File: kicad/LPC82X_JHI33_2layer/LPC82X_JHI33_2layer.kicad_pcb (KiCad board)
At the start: 2 copper layers, 23.6 x 23.5 mm, 23 parts, among them J1 Conn_02x09_Odd_Even, J2 Conn_02x09_Odd_Even, J3 JTAG_2X05, U1 LPC824M201JHI33, Y1 12MHz

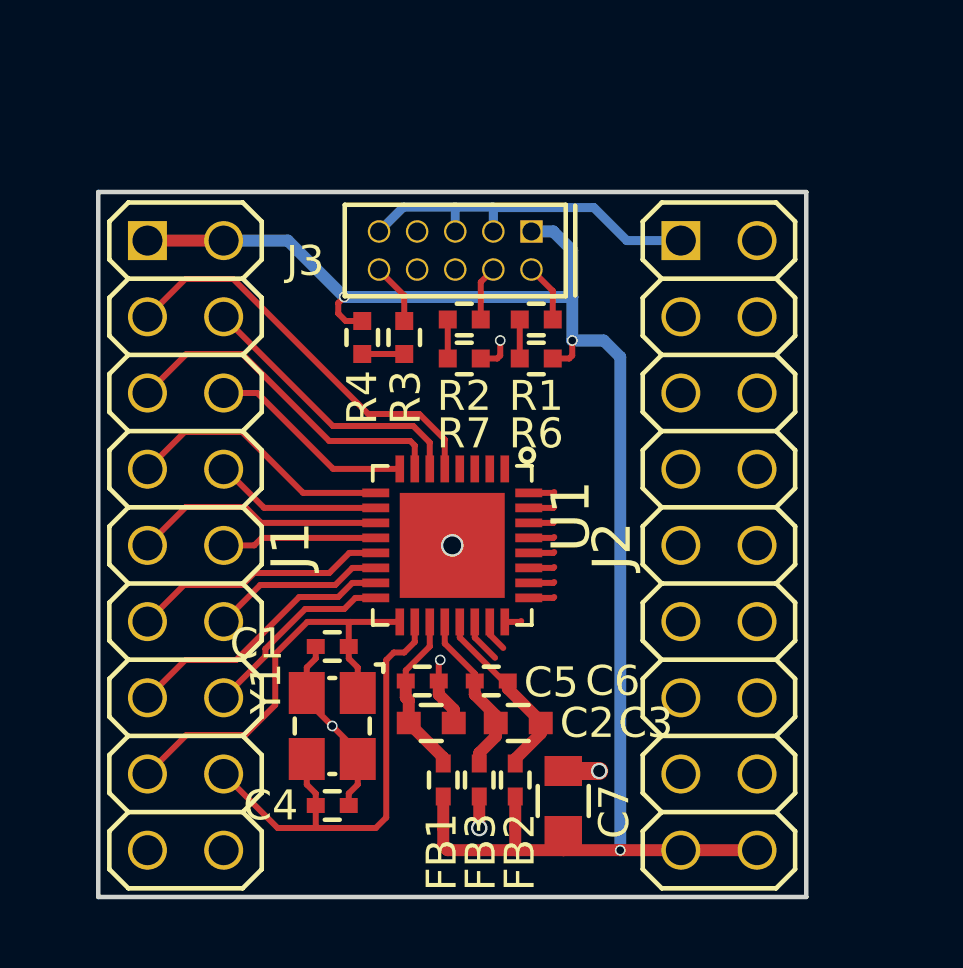
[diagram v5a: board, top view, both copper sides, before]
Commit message: updated schematic, added VDD jumper, added top groundplane, completed layout
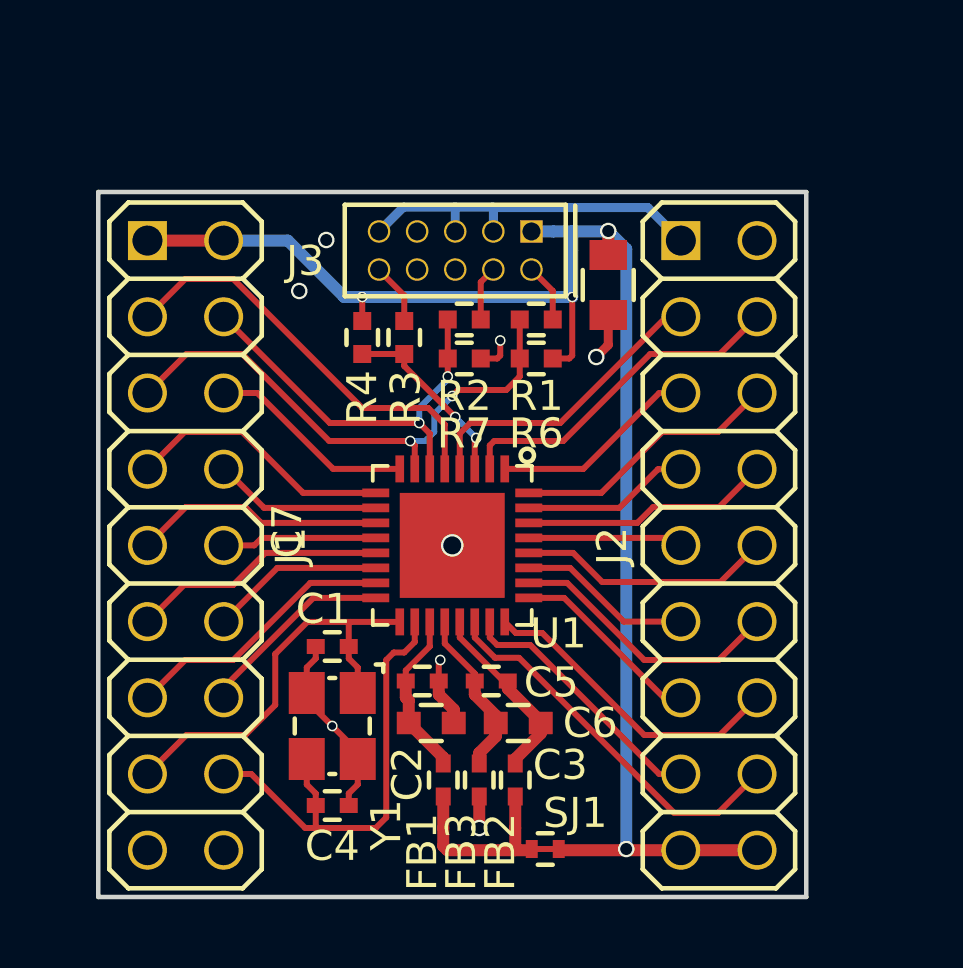
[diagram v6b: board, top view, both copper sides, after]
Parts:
- added SJ1: SolderJumper_2way_1conn, SquantorSpecial:solder_jumper_2way_conn, F.Cu at (92.0, 116.8)
- moved C7 17.3 mm to (94.1, 98.0), turned to 90 degrees
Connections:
- FB1 pad 2: VDD -> Net-(FB1-Pad2)
- FB2 pad 2: VDD -> Net-(FB1-Pad2)
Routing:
- net /PIO0_12: track 0.00 -> 11.5 mm
- net /PIO0_7: track 1.48 -> 12.9 mm
- net /PIO0_4: track 0.00 -> 10.2 mm
- net /PIO0_0: track 0.56 -> 10.5 mm
- net /PIO0_23: track 0.86 -> 9.20 mm
- net /PIO0_17: track 0.86 -> 8.99 mm
- net /PIO0_6: track 1.06 -> 8.77 mm
- net /PIO0_21: track 0.86 -> 8.52 mm
- net /PIO0_19: track 0.86 -> 8.35 mm
- net /PIO0_13: track 0.00 -> 6.92 mm
- net Net-(FB1-Pad2): track 0.00 -> 6.46 mm
- net /PIO0_14: track 0.86 -> 6.45 mm
- net /PIO0_2: track 12.8 -> 18.3 mm, vias 0 -> 2
- net /PIO0_22: track 0.86 -> 5.81 mm
- net /RESET: track 1.40 -> 6.24 mm, vias 0 -> 2
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- added copper zone on F.Cu, net VSS

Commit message: updated pcb and fixed some inconsistencies
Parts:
- moved C7 0.20 mm to (94.1, 98.2)
